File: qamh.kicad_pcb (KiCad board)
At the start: 2 copper layers, 40.3 x 128.5 mm, 19 parts, among them J1 Eurorack_Power_16pin_Shrouded, J2 OUTPUT, J3 INPUT 1, J4 INPUT 2, J5 INPUT 3, J6 Conn_01x02_Pin

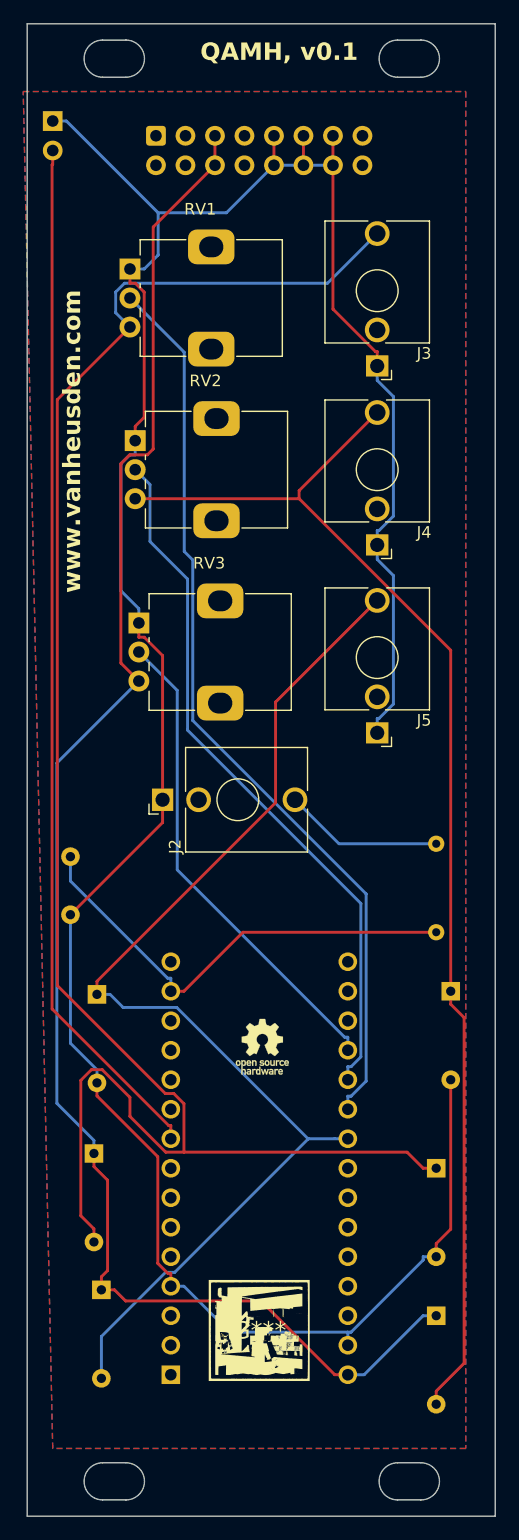
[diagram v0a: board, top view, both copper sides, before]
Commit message: replaced nano by pro mini
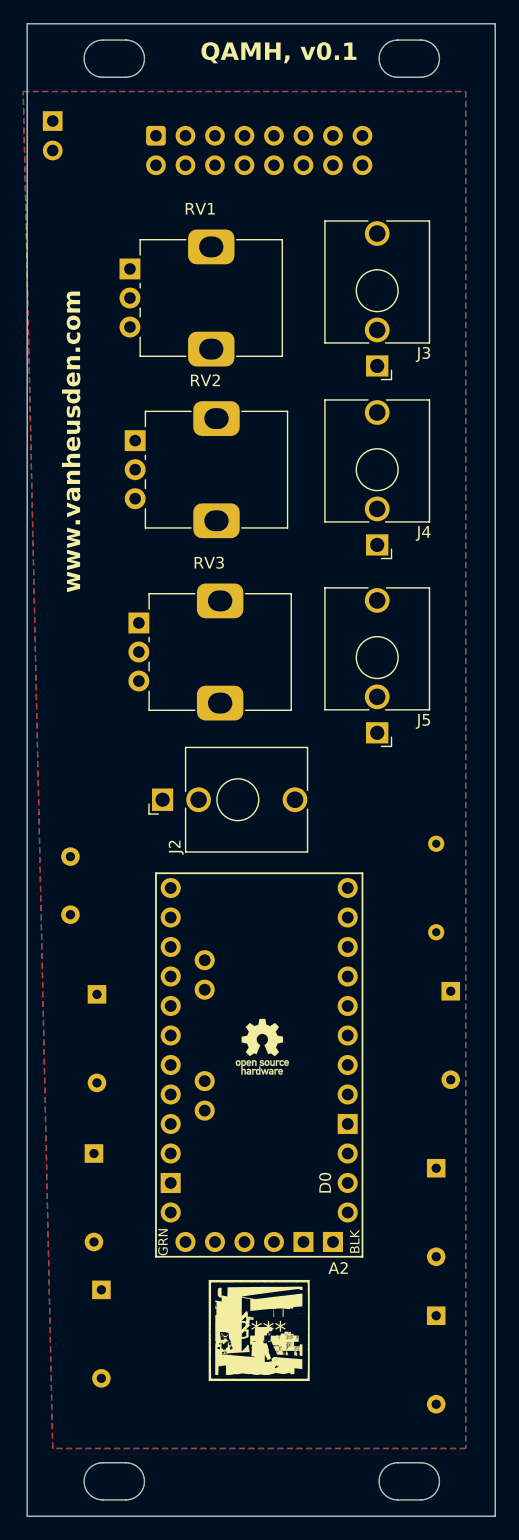
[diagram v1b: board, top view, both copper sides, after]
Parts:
- removed A1: Arduino_Nano_Every, Module:Arduino_Nano
- added A2: Arduino_Pro_Mini_Socket, PCM_arduino-library:Arduino_Pro_Mini_Socket, F.Cu at (221.0, 106.7)
- RV1: value P1 -> B10K (linear 10k ohm)
- RV2: value P2 -> B10K
- RV3: value P3 -> B10K
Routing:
- net GND: track 238.8 -> 0.00 mm
- net Net-(D1-A): track 156.6 -> 0.00 mm
- net +5V: track 143.2 -> 0.00 mm
- net Net-(D5-A): track 109.2 -> 0.00 mm
- net Net-(D3-A): track 99.1 -> 0.00 mm
- net Net-(J6-Pin_2): track 89.5 -> 0.00 mm
- net Net-(A2-PadA2): track 79.1 -> 0.00 mm
- net Net-(A2-PadA1): track 61.2 -> 0.00 mm
- net Net-(A2-PadA0): track 41.9 -> 0.00 mm
- net Net-(A2-D11_MOSI): track 40.3 -> 0.00 mm
- net Net-(J2-PadT): track 13.7 -> 0.00 mm

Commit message: arduino pro-mini layout
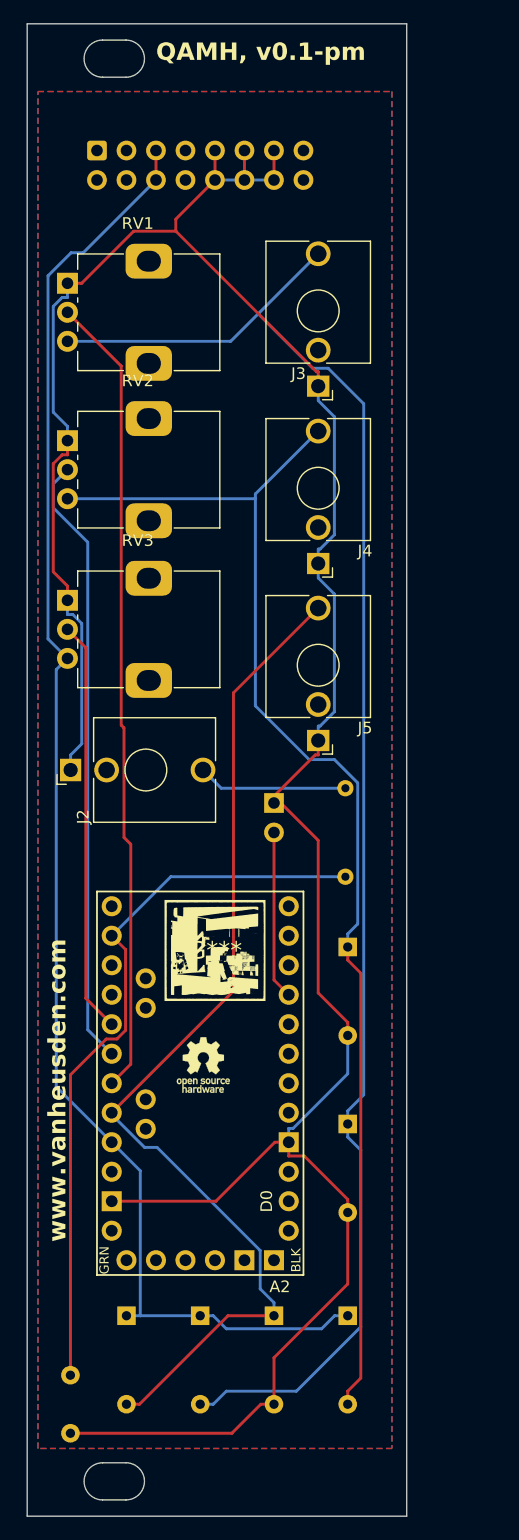
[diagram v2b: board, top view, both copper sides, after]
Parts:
- moved J6 61.7 mm to (222.2, 84.1)
- moved C1 44.6 mm to (204.7, 133.4)
- moved G*** 32.9 mm to (217.2, 96.8)
- moved D4 31.6 mm to (222.2, 128.3)
- moved D1 16.7 mm to (215.9, 128.3)
- moved D6 9.65 mm to (228.6, 96.5)
- moved R1 9.17 mm to (228.4, 82.8)
- moved D2 8.52 mm to (228.6, 111.8)
- moved J2 8.32 mm to (204.7, 81.3)
- moved D5 7.62 mm to (228.6, 128.3)
- moved RV3 6.45 mm to (204.5, 66.7)
- moved RV2 5.83 mm to (204.5, 52.9)
- moved RV1 5.52 mm to (204.5, 39.4)
- moved J3 5.37 mm to (226.1, 48.2)
- moved J4 5.33 mm to (226.1, 63.5)
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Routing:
- net GND: track 0.00 -> 232.7 mm
- net Net-(D1-A): track 0.00 -> 134.1 mm
- net +5V: track 0.00 -> 128.9 mm
- net Net-(D5-A): track 0.00 -> 108.4 mm
- net Net-(D3-A): track 0.00 -> 90.6 mm
- net Net-(A2-PadA2): track 0.00 -> 69.3 mm
- net Net-(A2-D11_MOSI): track 0.00 -> 63.1 mm
- net Net-(A2-PadA1): track 0.00 -> 52.9 mm
- net Net-(A2-PadA0): track 0.00 -> 35.6 mm
- net Net-(J6-Pin_2): track 0.00 -> 14.5 mm
- net Net-(J2-PadT): track 0.00 -> 12.9 mm
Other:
- board size 40.3 x 128.5 mm -> 32.7 x 128.5 mm
- board text added: "QAMH, v0.1-pm"
- board text removed: "QAMH, v0.1"
